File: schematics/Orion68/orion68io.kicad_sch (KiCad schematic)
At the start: 48 parts, among them IC4 XR68C681CJTR-F, J1 LevelConverter, J200 Euro96pin, J22 Kbd_usb, J23 Conn_01x06, Q4 3.6864MHz, U200 GAL16V8, U25 SN74LVC245APW, U26 SN74LVC245APW, U27 RP5C01A, U30 LM2937xT, U33 68681, Y3 Crystal

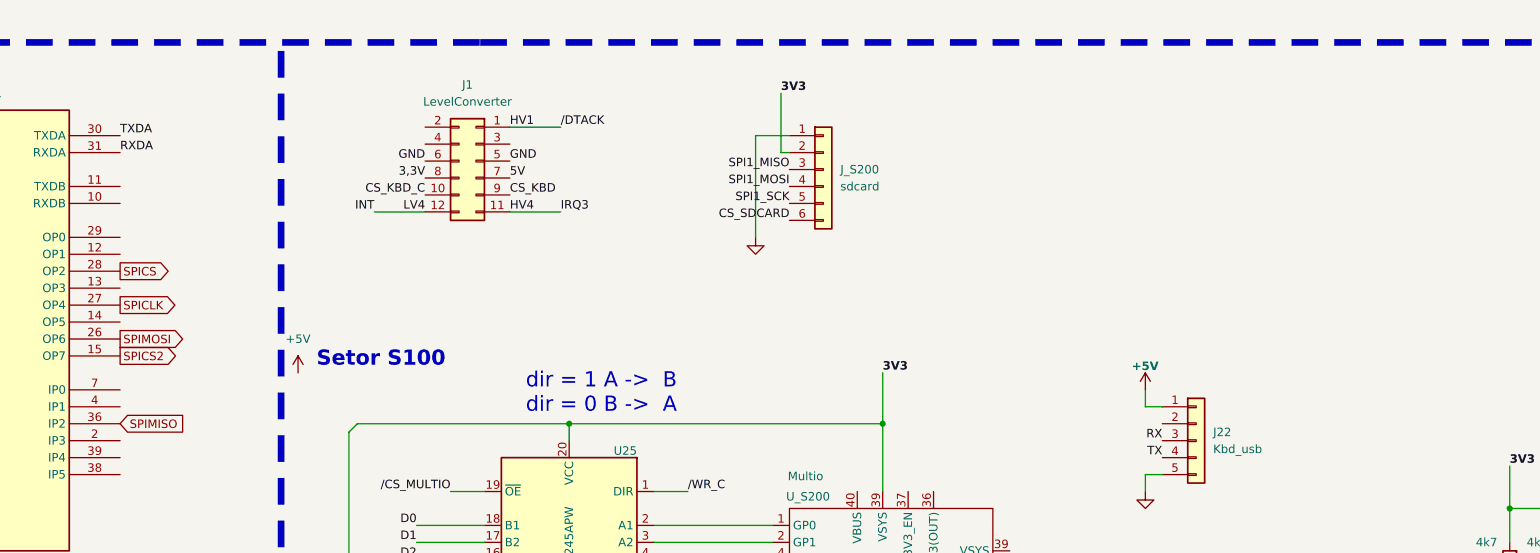
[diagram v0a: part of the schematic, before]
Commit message: Duart A e B running OK.
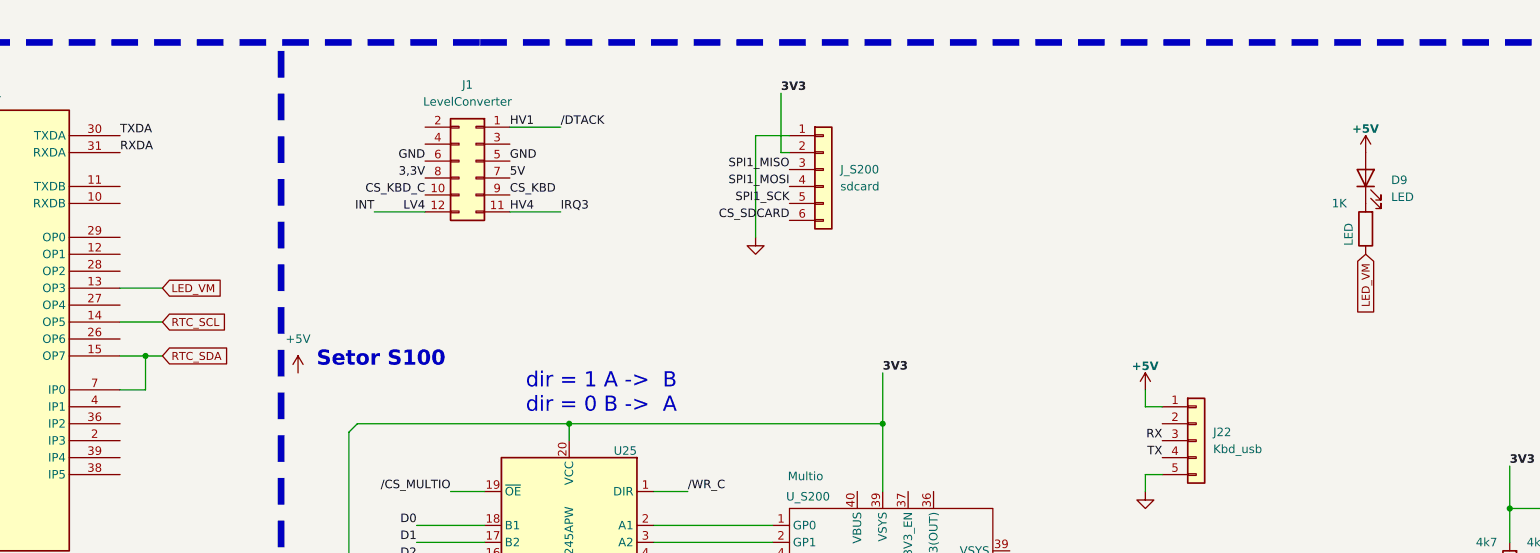
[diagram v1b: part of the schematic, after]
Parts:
- added D9: LED, symbol Device:LED
- added LED: 1K, Resistor_THT:R_Axial_DIN0204_L3.6mm_D1.6mm_P5.08mm_Horizontal, symbol Device:R
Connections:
- net +5V: now also D9.2 (A)
- net SPICLK: no longer U33.27 (OP4)
- net SPICS: no longer U33.28 (OP2)
- net SPICS2: no longer U33.15 (OP7)
- net SPIMISO: no longer U33.36 (IP2)
- net SPIMOSI: no longer U33.26 (OP6)
- net LED_VM: now reaches U33.13 (OP3)
- net LED_VM: now also LED.1
- net RTC_SCL: now reaches U33.14 (OP5)
- net RTC_SDA: now reaches U33.7 (IP0)
- net RTC_SDA: now also U33.15 (OP7)
- new net: D9.1 (K), LED.2

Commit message: Duart A running well
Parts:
- removed BT1: Battery, symbol Device:Battery
- removed C1: 100nF, symbol Device:C
- removed C11: 6,8pF a 45pF, symbol Device:C_Trim
- removed C12: 56pF, symbol Device:C
- removed C13: 22pF, symbol Device:C
- removed D6, D8: 1N5819, Diode_SMD:D_SOD-523, symbol Diode:1N4148WT
- removed R17: 1k2, symbol Device:R
- removed R18: 100k, symbol Device:R
- removed R55: 10k, symbol Device:R
- removed U27: RP5C01A, symbol pdSilva:RP5C01A
- removed Y3: Crystal, symbol Device:Crystal
- added C1, C12, C4, C6: 1uf, symbol Device:C_Polarized
- added J26: DuartB, symbol Connector_Generic:Conn_02x05_Odd_Even
- added J28: DuartA, symbol Connector_Generic:Conn_02x05_Odd_Even
- added U36: UART2, symbol Interface_UART:MAX232
- C2: renamed from C10; value 4,7uF -> 1uf
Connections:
- net +5V: now also C12.1, U36.16 (VCC)
- net GND: now also J26.5 (Pin_5), J28.5 (Pin_5); no longer C2.2
- net RXDA: no longer U33.31 (RXDA)
- net TXDA: no longer U33.30 (TXDA)
- net at C2.1: now also U36.2 (VS+)
- net RXB: now reaches U33.10 (RXDB)
- net RXB: now also U36.9 (R2OUT)
- net TXB: now reaches U33.11 (TXDB)
- net TXB: now also U36.10 (T2IN)
- new net: C4.1, U36.4 (C2+)
- new net: C4.2, U36.5 (C2-)
- new net: C1.1, U36.1 (C1+)
- new net: C1.2, U36.3 (C1-)
- new net: C6.2, U36.6 (VS-)
- new net GNDREF: C12.2, C2.2, C6.1, U36.15 (GND)
- new net RX1: J28.2 (Pin_2), U36.13 (R1IN)
- new net RX2: J26.2 (Pin_2), U36.8 (R2IN)
- new net RXA: U33.31 (RXDA), U36.12 (R1OUT)
- new net TX1: J28.3 (Pin_3), U36.14 (T1OUT)
- new net TX2: J26.3 (Pin_3), U36.7 (T2OUT)
- new net TXA: U33.30 (TXDA), U36.11 (T1IN)
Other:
- note added: "FF9000->DUART -Uart1 FF9100->Super MultiIO FF9200->RTC RP5C01A da Ricoh"
- note removed: "FF9000->DUART -Uart1 = Keyboard USB Uart2=livre FF9100->Super MultiIO FF9200->RTC RP5C01A da Ricoh"
- moved on the sheet: C2, D9, J22, LED
